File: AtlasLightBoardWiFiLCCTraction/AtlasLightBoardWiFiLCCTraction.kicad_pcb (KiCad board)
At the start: 2 copper layers, 76.7 x 20.3 mm, 41 parts, among them IC101 REG1117-3.3_2K5G4, IC102 MP6614GN-Z, J101 USB_C_Receptacle, SW101 Reset, SW102 Boot, U101 ESP32_S3_WROOM, U102 TBD62083A

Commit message: PCB Completed.
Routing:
- net Net-(D102-Pad3): track 55.1 -> 53.6 mm
- net Net-(R105-Pad1): track 56.8 -> 55.4 mm
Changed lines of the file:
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@@
   (segment (start 123.19 87.249) (end 123.19 85.258) (width 1) (layer "F.Cu") (net 7))
   (segment (start 123.19 85.258) (end 122.609 84.677) (width 1) (layer "F.Cu") (net 7))
+  (segment (start 111.039 84.541) (end 111.039 84.633702) (width 1) (layer "B.Cu") (net 7))
+  (segment (start 77.724 86.741) (end 79.383 88.4) (width 1) (layer "B.Cu") (net 7))
+  (segment (start 114.416298 88.011) (end 122.428 88.011) (width 1) (layer "B.Cu") (net 7))
+  (segment (start 111.039 84.633702) (end 114.416298 88.011) (width 1) (layer "B.Cu") (net 7))
   (segment (start 79.383 88.4) (end 98.589 88.4) (width 1) (layer "B.Cu") (net 7))
+  (segment (start 98.589 88.4) (end 102.448 84.541) (width 1) (layer "B.Cu") (net 7))
+  (segment (start 76.454 86.741) (end 77.724 86.741) (width 1) (layer "B.Cu") (net 7))
+  (segment (start 122.428 88.011) (end 123.19 87.249) (width 1) (layer "B.Cu") (net 7))
   (segment (start 102.448 84.541) (end 111.039 84.541) (width 1) (layer "B.Cu") (net 7))
-  (segment (start 76.454 86.741) (end 77.724 86.741) (width 1) (layer "B.Cu") (net 7))
-  (segment (start 111.039 84.541) (end 111.039 87.63) (width 1) (layer "B.Cu") (net 7))
-  (segment (start 122.809 87.63) (end 123.19 87.249) (width 1) (layer "B.Cu") (net 7))
-  (segment (start 111.039 87.63) (end 122.809 87.63) (width 1) (layer "B.Cu") (net 7))
-  (segment (start 77.724 86.741) (end 79.383 88.4) (width 1) (layer "B.Cu") (net 7))
-  (segment (start 98.589 88.4) (end 102.448 84.541) (width 1) (layer "B.Cu") (net 7))
   (segment (start 123.952 70.231) (end 123.952 79.334) (width 1) (layer "F.Cu") (net 8))
   (segment (start 123.952 79.334) (end 122.609 80.677) (width 1) (layer "F.Cu") (net 8))
@@
   (via (at 81.28 84.963) (size 0.8) (drill 0.4) (layers "F.Cu" "B.Cu") (net 25))
   (via (at 126.746 87.757) (size 0.8) (drill 0.4) (layers "F.Cu" "B.Cu") (net 25))
+  (segment (start 119.839726 85.924) (end 118.958726 86.805) (width 0.25) (layer "B.Cu") (net 25))
+  (segment (start 100.097274 85.725) (end 90.814305 85.725) (width 0.25) (layer "B.Cu") (net 25))
+  (segment (start 90.033695 85.725) (end 82.042 85.725) (width 0.25) (layer "B.Cu") (net 25))
   (segment (start 90.123695 85.635) (end 90.033695 85.725) (width 0.25) (layer "B.Cu") (net 25))
+  (segment (start 112.249 84.747686) (end 112.249 84.584274) (width 0.25) (layer "B.Cu") (net 25))
+  (segment (start 114.306314 86.805) (end 112.249 84.747686) (width 0.25) (layer "B.Cu") (net 25))
+  (segment (start 90.724305 85.635) (end 90.123695 85.635) (width 0.25) (layer "B.Cu") (net 25))
+  (segment (start 111.380726 83.716) (end 102.106274 83.716) (width 0.25) (layer "B.Cu") (net 25))
+  (segment (start 118.958726 86.805) (end 114.306314 86.805) (width 0.25) (layer "B.Cu") (net 25))
+  (segment (start 112.249 84.584274) (end 111.380726 83.716) (width 0.25) (layer "B.Cu") (net 25))
   (segment (start 90.814305 85.725) (end 90.724305 85.635) (width 0.25) (layer "B.Cu") (net 25))
-  (segment (start 111.864 86.805) (end 111.864 84.199274) (width 0.25) (layer "B.Cu") (net 25))
-  (segment (start 119.839726 85.924) (end 118.958726 86.805) (width 0.25) (layer "B.Cu") (net 25))
-  (segment (start 90.033695 85.725) (end 82.042 85.725) (width 0.25) (layer "B.Cu") (net 25))
-  (segment (start 111.864 84.199274) (end 111.380726 83.716) (width 0.25) (layer "B.Cu") (net 25))
+  (segment (start 124.913 85.924) (end 119.839726 85.924) (width 0.25) (layer "B.Cu") (net 25))
+  (segment (start 126.746 87.757) (end 124.913 85.924) (width 0.25) (layer "B.Cu") (net 25))
   (segment (start 82.042 85.725) (end 81.28 84.963) (width 0.25) (layer "B.Cu") (net 25))
-  (segment (start 118.958726 86.805) (end 111.864 86.805) (width 0.25) (layer "B.Cu") (net 25))
-  (segment (start 100.097274 85.725) (end 90.814305 85.725) (width 0.25) (layer "B.Cu") (net 25))
-  (segment (start 90.724305 85.635) (end 90.123695 85.635) (width 0.25) (layer "B.Cu") (net 25))
   (segment (start 102.106274 83.716) (end 100.097274 85.725) (width 0.25) (layer "B.Cu") (net 25))
-  (segment (start 124.913 85.924) (end 119.839726 85.924) (width 0.25) (layer "B.Cu") (net 25))
-  (segment (start 111.380726 83.716) (end 102.106274 83.716) (width 0.25) (layer "B.Cu") (net 25))
-  (segment (start 126.746 87.757) (end 124.913 85.924) (width 0.25) (layer "B.Cu") (net 25))
   (segment (start 85.951 84.612) (end 85.473 85.09) (width 0.25) (layer "F.Cu") (net 26))
   (segment (start 86.741 84.612) (end 85.951 84.612) (width 0.25) (layer "F.Cu") (net 26))

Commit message: PCB Completed.
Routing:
- net /Function1: track 69.5 -> 68.0 mm, vias 6 -> 4
- net Net-(R105-Pad1): track 55.4 -> 56.0 mm

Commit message: PCB Completed.
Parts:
- moved D101 2.36 mm to (96.9, 73.3), turned to 180 degrees
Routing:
- net /VBus: track 30.2 -> 32.9 mm
- net GND: track 112.5 -> 111.4 mm
- net /Vin: track 9.16 -> 8.47 mm
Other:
- board text added: "F"

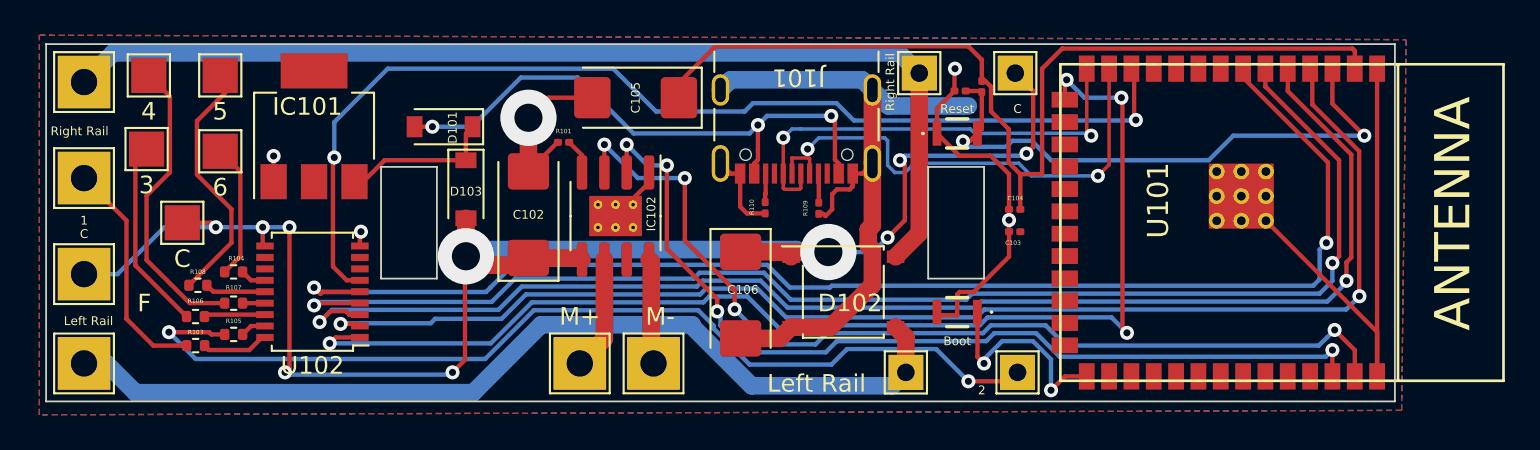
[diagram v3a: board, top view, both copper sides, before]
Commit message: Adjust things to increase heatsinking for 3.3 regulator.
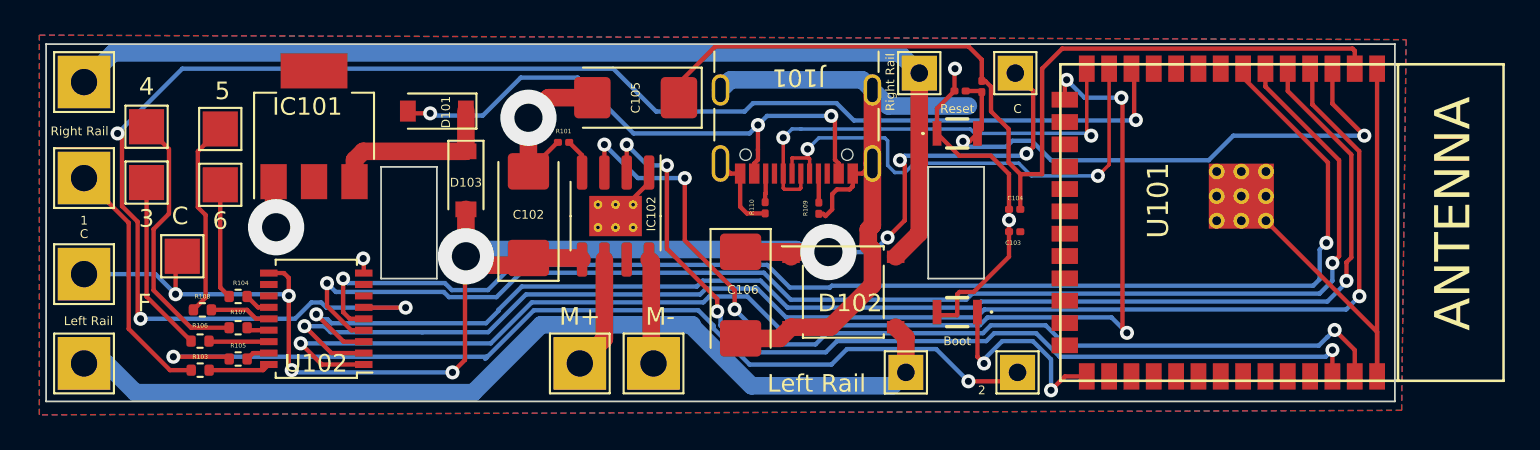
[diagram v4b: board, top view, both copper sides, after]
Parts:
- moved TP116 3.05 mm to (84.2, 73.4)
- moved TP115 2.92 mm to (80.0, 73.3)
- moved TP107 1.91 mm to (82.0, 80.6)
- moved TP111 1.91 mm to (84.2, 76.6)
- moved TP114 1.90 mm to (80.0, 76.5)
- moved U102 1.55 mm to (89.7, 84.2)
- moved R103 1.42 mm to (83.1, 87.1)
- moved R106 1.42 mm to (83.1, 85.5)
- moved R107 1.42 mm to (85.2, 84.7)
- moved R104 1.42 mm to (85.2, 82.9)
- moved R105 1.42 mm to (85.2, 86.5)
- moved R108 1.42 mm to (83.2, 83.7)
- moved D101 0.97 mm to (96.5, 72.4)
- moved D103 0.51 mm to (98.2, 76.3)
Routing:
- net /Function6: track 61.6 -> 93.1 mm, vias 2 -> 4
- net /Function2: track 75.2 -> 80.6 mm
- net /Function1: track 68.0 -> 71.8 mm
- net Net-(R108-Pad1): track 14.8 -> 11.3 mm
- net /MPower: track 98.0 -> 95.1 mm, vias 10 -> 9
- net Net-(R107-Pad1): track 17.0 -> 15.4 mm
- net /Vin: track 8.47 -> 10.1 mm
- net GND: track 111.4 -> 112.6 mm
- net /Function3: track 77.0 -> 78.2 mm
- net Net-(R104-Pad1): track 7.70 -> 6.56 mm
- net /Function5: track 75.6 -> 74.5 mm
- net Net-(R103-Pad1): track 13.1 -> 14.2 mm
- net Net-(R106-Pad1): track 11.0 -> 10.1 mm
- net Net-(R105-Pad1): track 56.0 -> 55.2 mm
- net /Function4: track 76.4 -> 77.1 mm

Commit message: Replace LDO with switching PS.
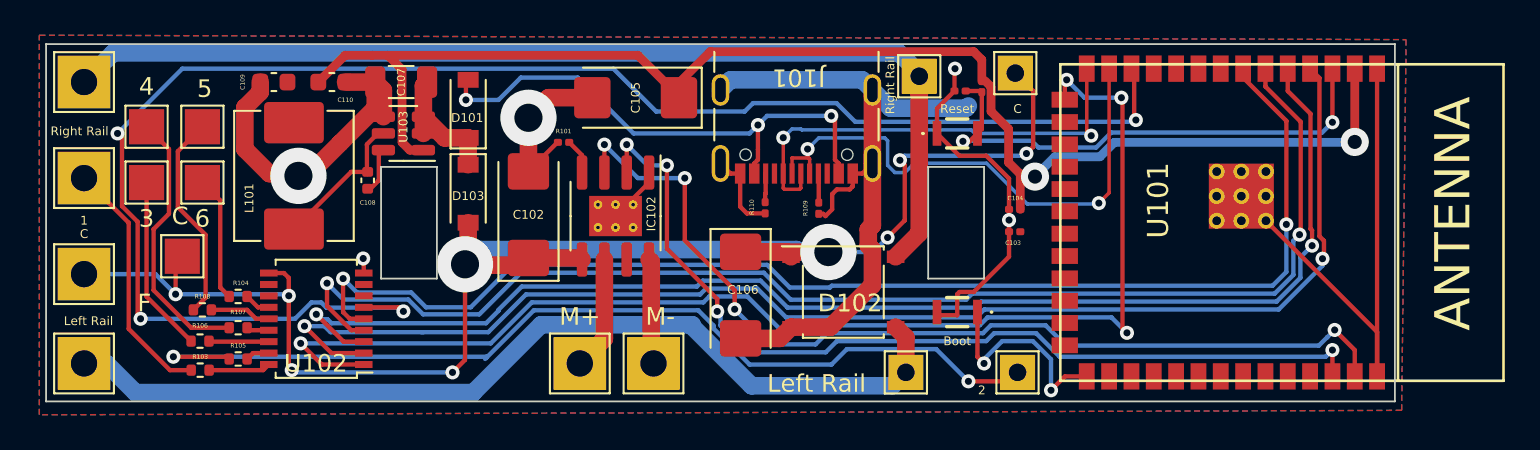
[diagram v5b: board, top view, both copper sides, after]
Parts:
- removed IC101: REG1117-3.3_2K5G4, Package_TO_SOT_SMD:SOT-223-3_TabPin2
- added C107: 10uf 25V, Capacitor_SMD:C_1206_3216Metric, F.Cu at (94.5, 70.7)
- added C108: 100nf, Capacitor_SMD:C_0402_1005Metric, F.Cu at (92.6, 76.3)
- added C109: 22uf 6.3V, Capacitor_SMD:C_0603_1608Metric, F.Cu at (87.2, 70.7)
- added C110: 22uf 6.3V, Capacitor_SMD:C_0603_1608Metric, F.Cu at (90.6, 70.7)
- added L101: 3.9uH, Inductor_SMD:L_Abracon_ASPI-0630LR, F.Cu at (88.4, 76.1)
- added U103: AP63203WU, Package_TO_SOT_SMD:TSOT-23-6, F.Cu at (94.6, 73.7)
- moved D101 1.78 mm to (98.3, 72.3), turned to 90 degrees
- moved TP111 1.02 mm to (83.2, 76.5)
- moved TP116 1.02 mm to (83.2, 73.3)
- moved D103 0.77 mm to (98.3, 77.1)
- moved TP121 0.18 mm to (124.0, 70.4)
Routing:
- net +3V3: track 54.7 -> 82.0 mm, vias 0 -> 2
- net GND: track 112.6 -> 129.0 mm
- net Net-(C108-Pad1): track 0.00 -> 8.76 mm
- net /Function2: track 80.6 -> 76.7 mm
- net /Reset: track 33.1 -> 29.2 mm
- net /Function3: track 78.2 -> 74.6 mm
- net Net-(C108-Pad2): track 0.00 -> 2.66 mm
- net /VBus: track 33.1 -> 30.5 mm
- net /Function5: track 74.5 -> 72.0 mm
- net /Function4: track 77.1 -> 74.6 mm
- net /Vin: track 10.1 -> 7.58 mm
- net /D-: track 28.5 -> 30.8 mm
- net Net-(D102-Pad4): track 59.7 -> 60.7 mm
- net Net-(R108-Pad1): track 11.3 -> 11.9 mm
- net /MPower: track 95.1 -> 94.4 mm
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
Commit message: Add Keep Alive connection.
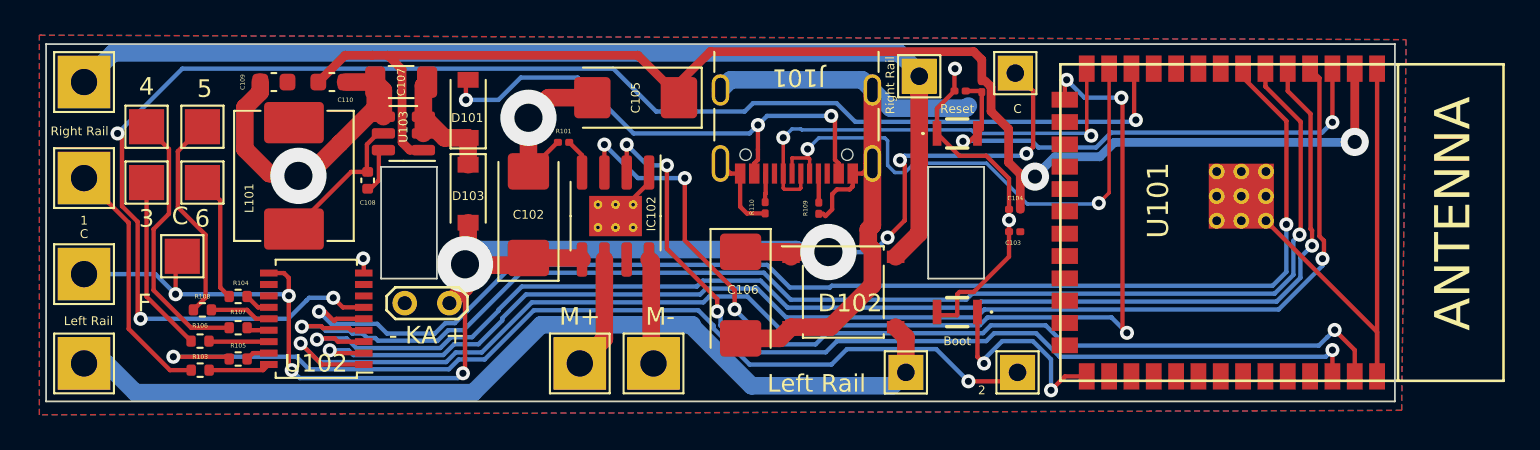
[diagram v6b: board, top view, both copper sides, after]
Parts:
- added TP104: - KA +, TestPoint:TestPoint_2Pads_Pitch2.54mm_Drill0.8mm, F.Cu at (94.7, 83.3)
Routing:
- net /Function6: track 93.1 -> 88.6 mm
- net /MPower: track 94.4 -> 97.5 mm
- net /Function2: track 76.7 -> 73.7 mm
- net /Function5: track 72.0 -> 73.5 mm
- net /Function4: track 74.6 -> 75.9 mm
- net /Function1: track 71.8 -> 72.7 mm

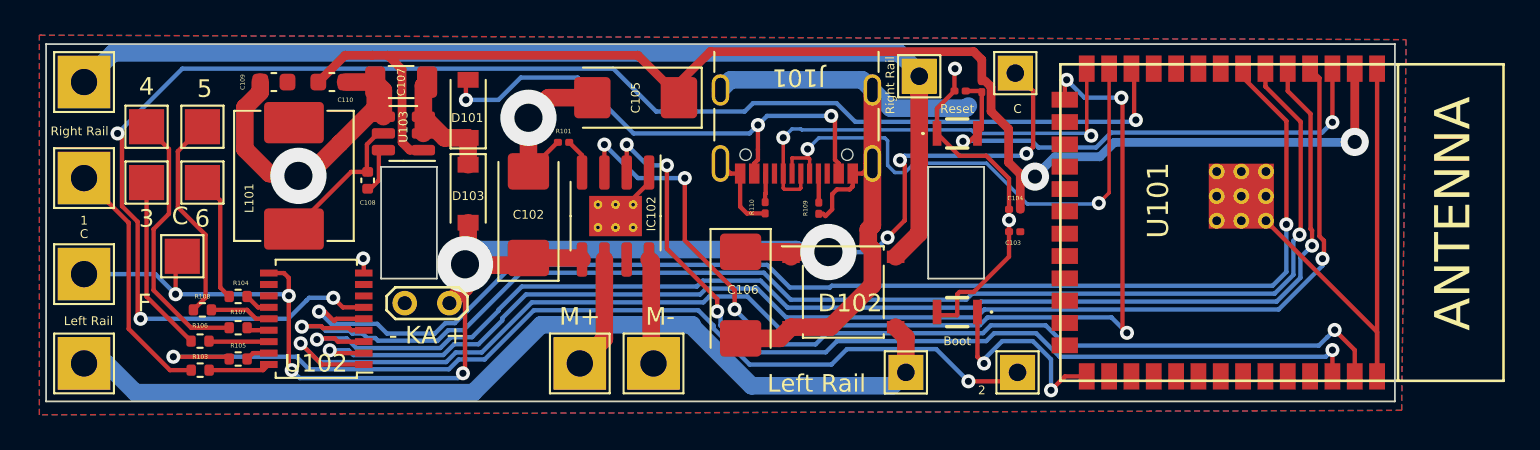
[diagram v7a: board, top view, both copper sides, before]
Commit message: Fine tune mounting hole positions (from accurate measurements).
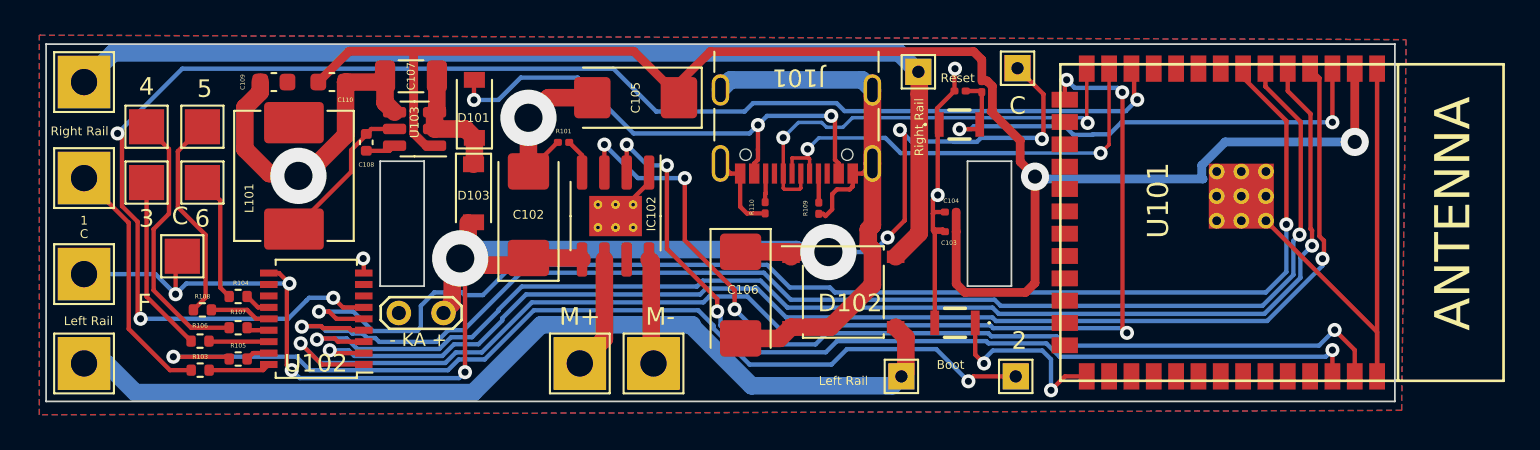
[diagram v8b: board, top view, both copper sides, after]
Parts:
- TP112, TP113, TP121, TP122: footprint TestPoint:TestPoint_THTPad_2.0x2.0mm_Drill1.0mm -> TestPoint:TestPoint_THTPad_1.5x1.5mm_Drill0.7mm
- moved C104 3.65 mm to (125.7, 78.1)
- moved C103 3.65 mm to (125.7, 79.2)
- moved C108 2.16 mm to (92.5, 74.2)
- moved U103 0.68 mm to (95.2, 73.4)
- moved TP104 0.65 mm to (94.4, 83.9)
- moved C107 0.65 mm to (95.0, 70.4)
- moved SW102 0.62 mm to (126.0, 84.4)
- moved SW101 0.52 mm to (126.2, 73.2)
- moved D101 0.36 mm to (98.7, 72.3)
- moved TP122 0.34 mm to (122.9, 87.5)
- moved TP112 0.31 mm to (129.5, 70.0)
- moved D103 0.31 mm to (98.6, 77.1)
- moved TP121 0.26 mm to (123.9, 70.2)
- moved TP113 0.25 mm to (129.4, 87.5)
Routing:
- net +3V3: track 82.0 -> 94.0 mm
- net GND: track 129.0 -> 120.3 mm
- net /D-: track 30.8 -> 25.5 mm
- net /MPower: track 97.5 -> 101.7 mm
- net /Function6: track 88.6 -> 87.6 mm
- net /Boot0: track 12.1 -> 11.1 mm
- net Net-(C108-Pad2): track 2.66 -> 1.73 mm
- net /Function5: track 73.5 -> 74.3 mm
- net /D+: track 26.5 -> 26.0 mm
- net /Vin: track 7.58 -> 7.05 mm
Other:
- outline, holes or cut-outs redrawn
